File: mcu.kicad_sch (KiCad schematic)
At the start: 17 parts, among them J2 SWD_HIL, U7 STM32G431RBT6

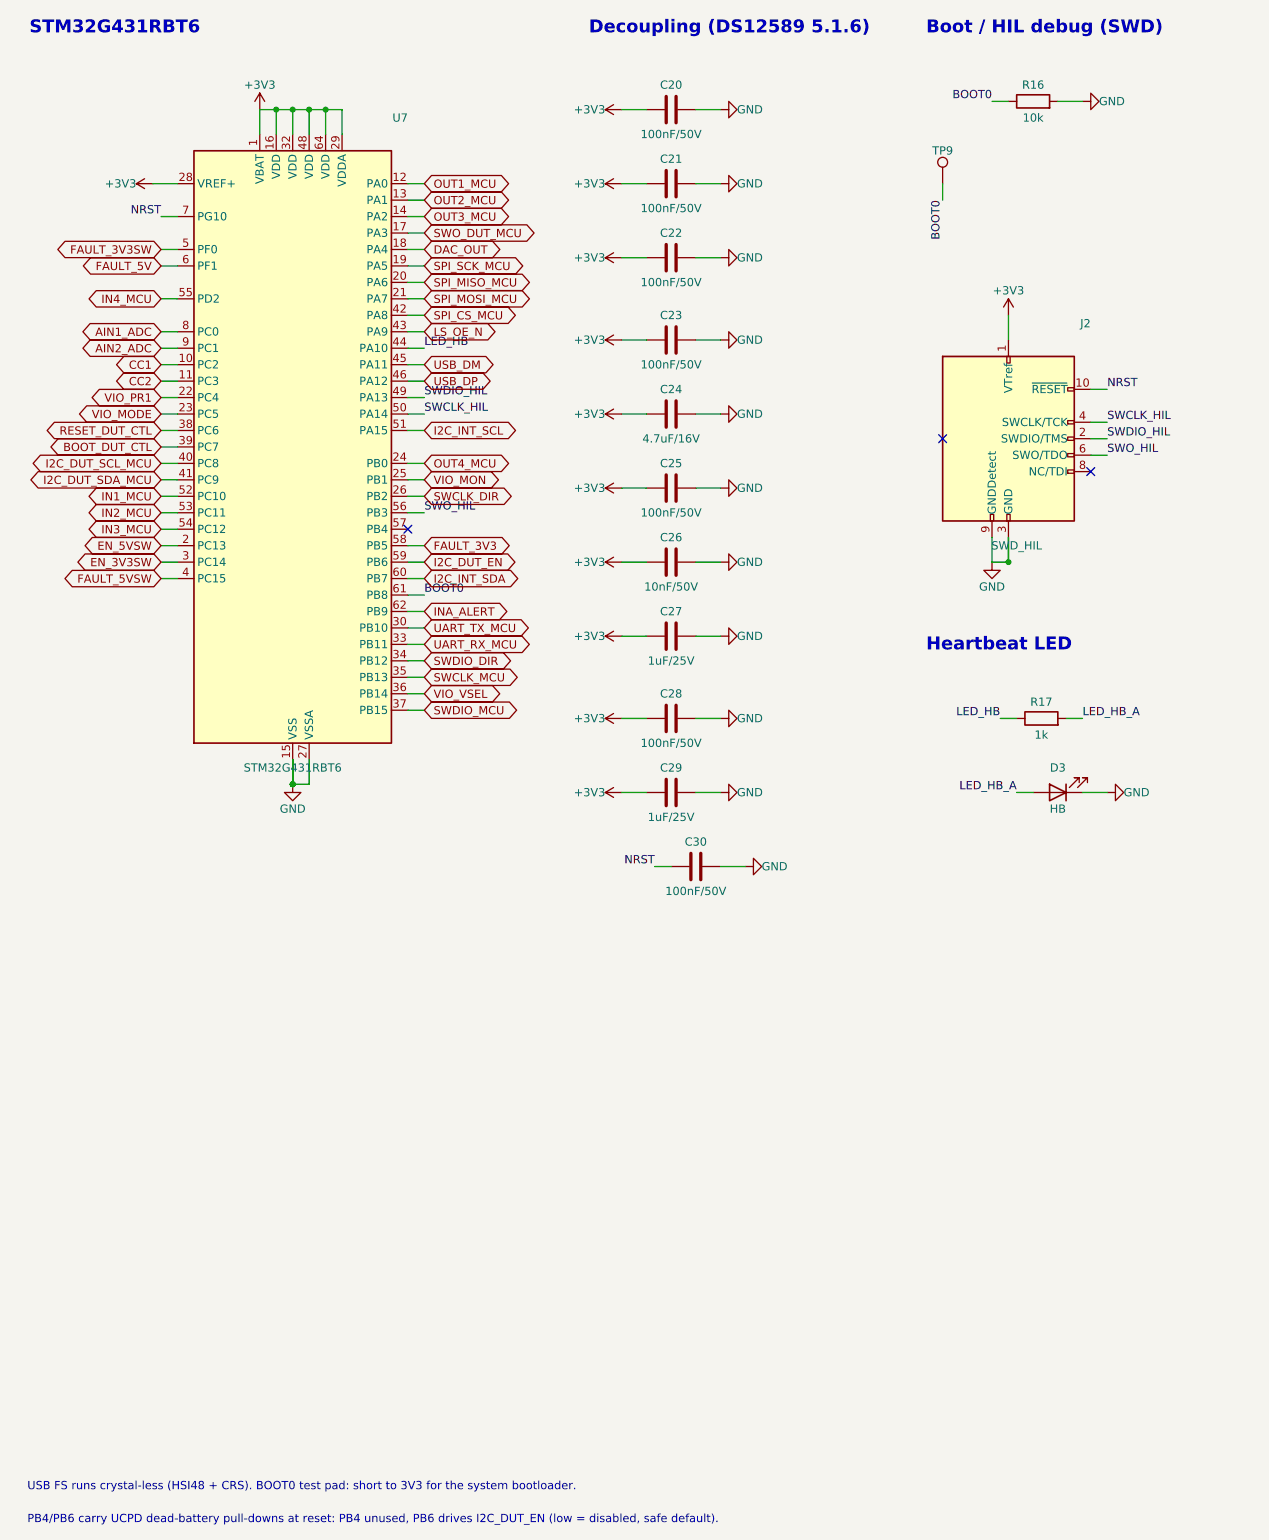
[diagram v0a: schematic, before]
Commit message: fix: apply schematic review findings (VIO 5V at power-up, push-pull BOOT, input bias, CC ESD)
Co-Authored-By: Claude Opus 5.5 <noreply@anthropic.com>
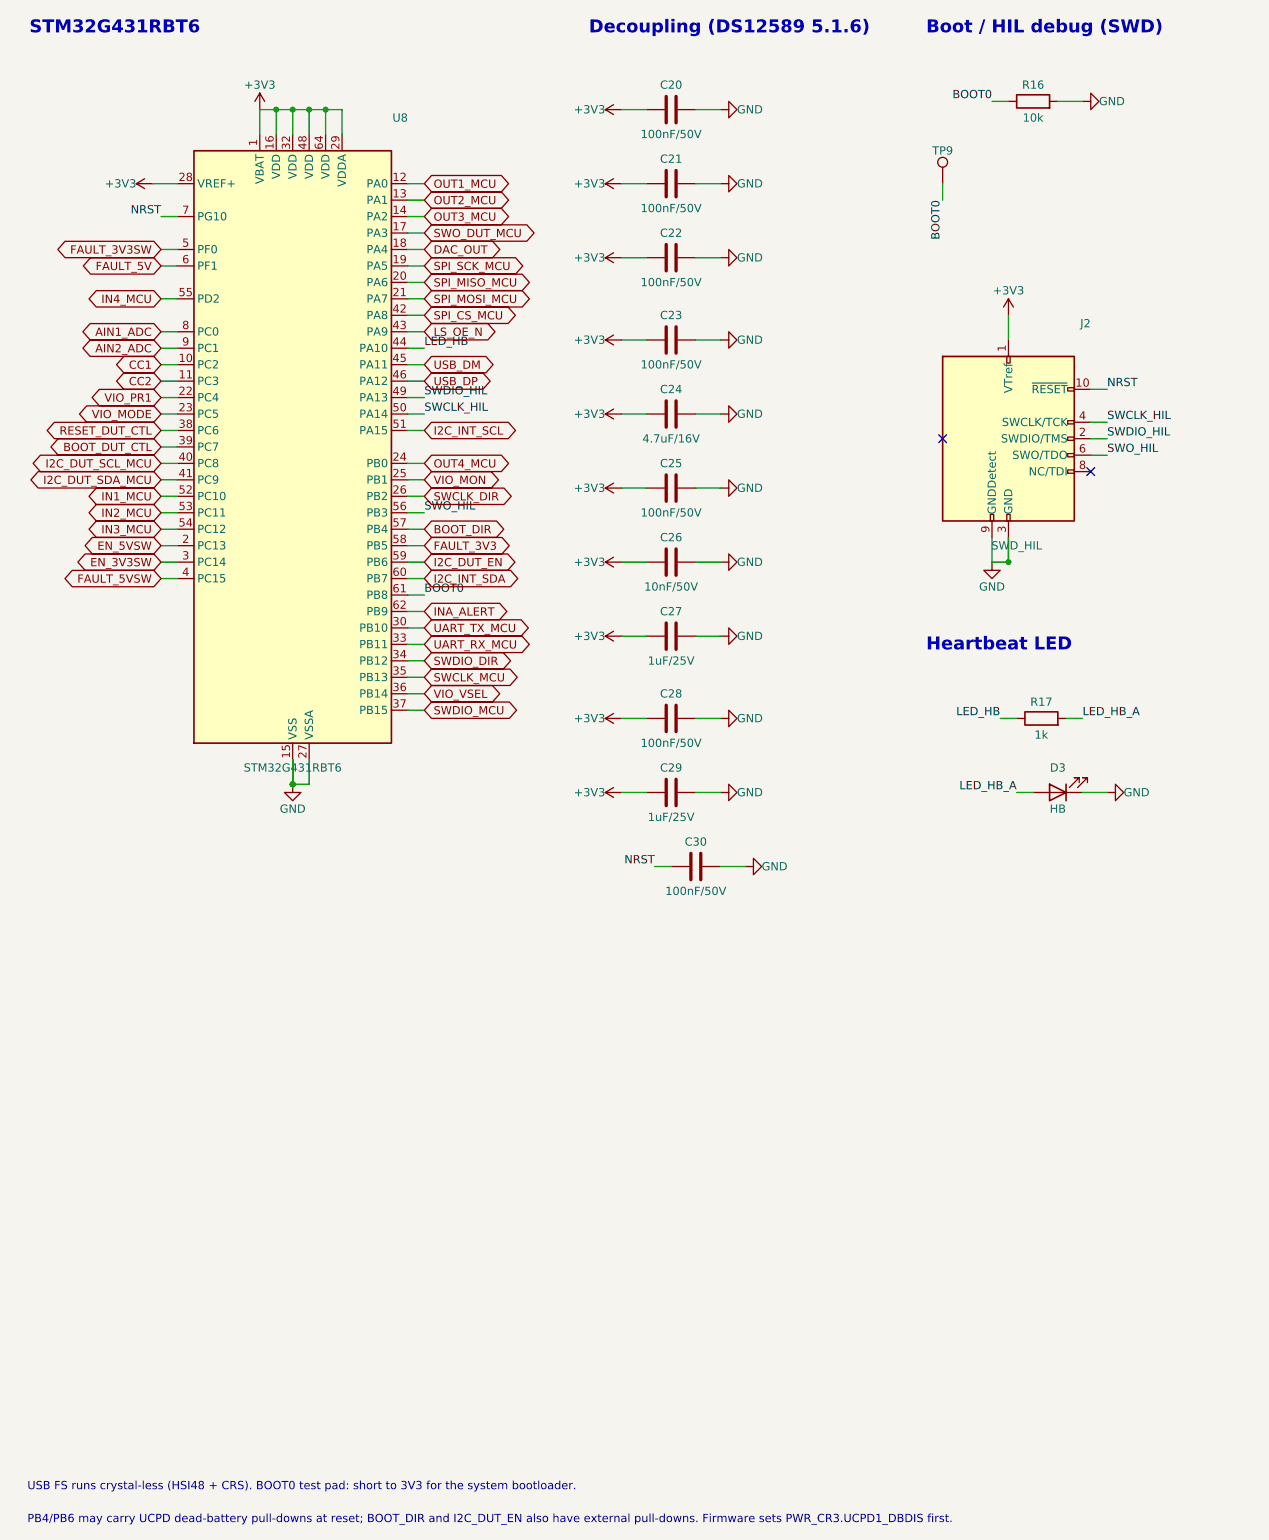
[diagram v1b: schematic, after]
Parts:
- removed U7: STM32G431RBT6, Package_QFP:LQFP-64_10x10mm_P0.5mm, symbol MCU_ST_STM32G4:STM32G431RBTx
- added U8: STM32G431RBT6, Package_QFP:LQFP-64_10x10mm_P0.5mm, symbol MCU_ST_STM32G4:STM32G431RBTx
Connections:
- net +3V3: now also U8.1 (VBAT), U8.16 (VDD), U8.28 (VREF+), U8.29 (VDDA), U8.32 (VDD), U8.48 (VDD), U8.64 (VDD)
- net AIN1_ADC: now also U8.8 (PC0)
- net AIN2_ADC: now also U8.9 (PC1)
- net BOOT0: now also U8.61 (PB8)
- net BOOT_DUT_CTL: now also U8.39 (PC7)
- net CC1: now also U8.10 (PC2)
- net CC2: now also U8.11 (PC3)
- net DAC_OUT: now also U8.18 (PA4)
- net EN_3V3SW: now also U8.3 (PC14)
- net EN_5VSW: now also U8.2 (PC13)
- net FAULT_3V3: now also U8.58 (PB5)
- net FAULT_3V3SW: now also U8.5 (PF0)
- net FAULT_5V: now also U8.6 (PF1)
- net FAULT_5VSW: now also U8.4 (PC15)
- net GND: now also U8.15 (VSS), U8.27 (VSSA), U8.31 (VSS), U8.47 (VSS), U8.63 (VSS)
- net I2C_DUT_EN: now also U8.59 (PB6)
- net I2C_DUT_SCL_MCU: now also U8.40 (PC8)
- net I2C_DUT_SDA_MCU: now also U8.41 (PC9)
- net I2C_INT_SCL: now also U8.51 (PA15)
- net I2C_INT_SDA: now also U8.60 (PB7)
- net IN1_MCU: now also U8.52 (PC10)
- net IN2_MCU: now also U8.53 (PC11)
- net IN3_MCU: now also U8.54 (PC12)
- net IN4_MCU: now also U8.55 (PD2)
- net INA_ALERT: now also U8.62 (PB9)
- net LED_HB: now also U8.44 (PA10)
- net LS_OE_N: now also U8.43 (PA9)
- net NRST: now also U8.7 (PG10)
- net OUT1_MCU: now also U8.12 (PA0)
- net OUT2_MCU: now also U8.13 (PA1)
- net OUT3_MCU: now also U8.14 (PA2)
- net OUT4_MCU: now also U8.24 (PB0)
- net RESET_DUT_CTL: now also U8.38 (PC6)
- net SPI_CS_MCU: now also U8.42 (PA8)
- net SPI_MISO_MCU: now also U8.20 (PA6)
- net SPI_MOSI_MCU: now also U8.21 (PA7)
- net SPI_SCK_MCU: now also U8.19 (PA5)
- net SWCLK_DIR: now also U8.26 (PB2)
- net SWCLK_HIL: now also U8.50 (PA14)
- net SWCLK_MCU: now also U8.35 (PB13)
- net SWDIO_DIR: now also U8.34 (PB12)
- net SWDIO_HIL: now also U8.49 (PA13)
- net SWDIO_MCU: now also U8.37 (PB15)
- net SWO_DUT_MCU: now also U8.17 (PA3)
- net SWO_HIL: now also U8.56 (PB3)
- net UART_RX_MCU: now also U8.33 (PB11)
- net UART_TX_MCU: now also U8.30 (PB10)
- net USB_DM: now also U8.45 (PA11)
- net USB_DP: now also U8.46 (PA12)
- net VIO_MODE: now also U8.23 (PC5)
- net VIO_MON: now also U8.25 (PB1)
- net VIO_PR1: now also U8.22 (PC4)
- net VIO_VSEL: now also U8.36 (PB14)
- new net BOOT_DIR: U8.57 (PB4)
- no-connect marks 3 -> 2
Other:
- note added: "PB4/PB6 may carry UCPD dead-battery pull-downs at reset; BOOT_DIR and I2C_DUT_EN also have external pull-downs. Firmware sets PWR_CR3.UCPD1_DBDIS first."
- note removed: "PB4/PB6 carry UCPD dead-battery pull-downs at reset: PB4 unused, PB6 drives I2C_DUT_EN (low = disabled, safe default)."
